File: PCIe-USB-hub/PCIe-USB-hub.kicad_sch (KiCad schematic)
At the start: 132 parts, among them J1 PCIexpress_x1, J2 USB3_A_Stacked, J3 USB3_A_Stacked, J4 USB3_A_Stacked, J5 USB3_A_Stacked, J6 USB3_A_Stacked, J7 Barrel_Jack_MountingPin

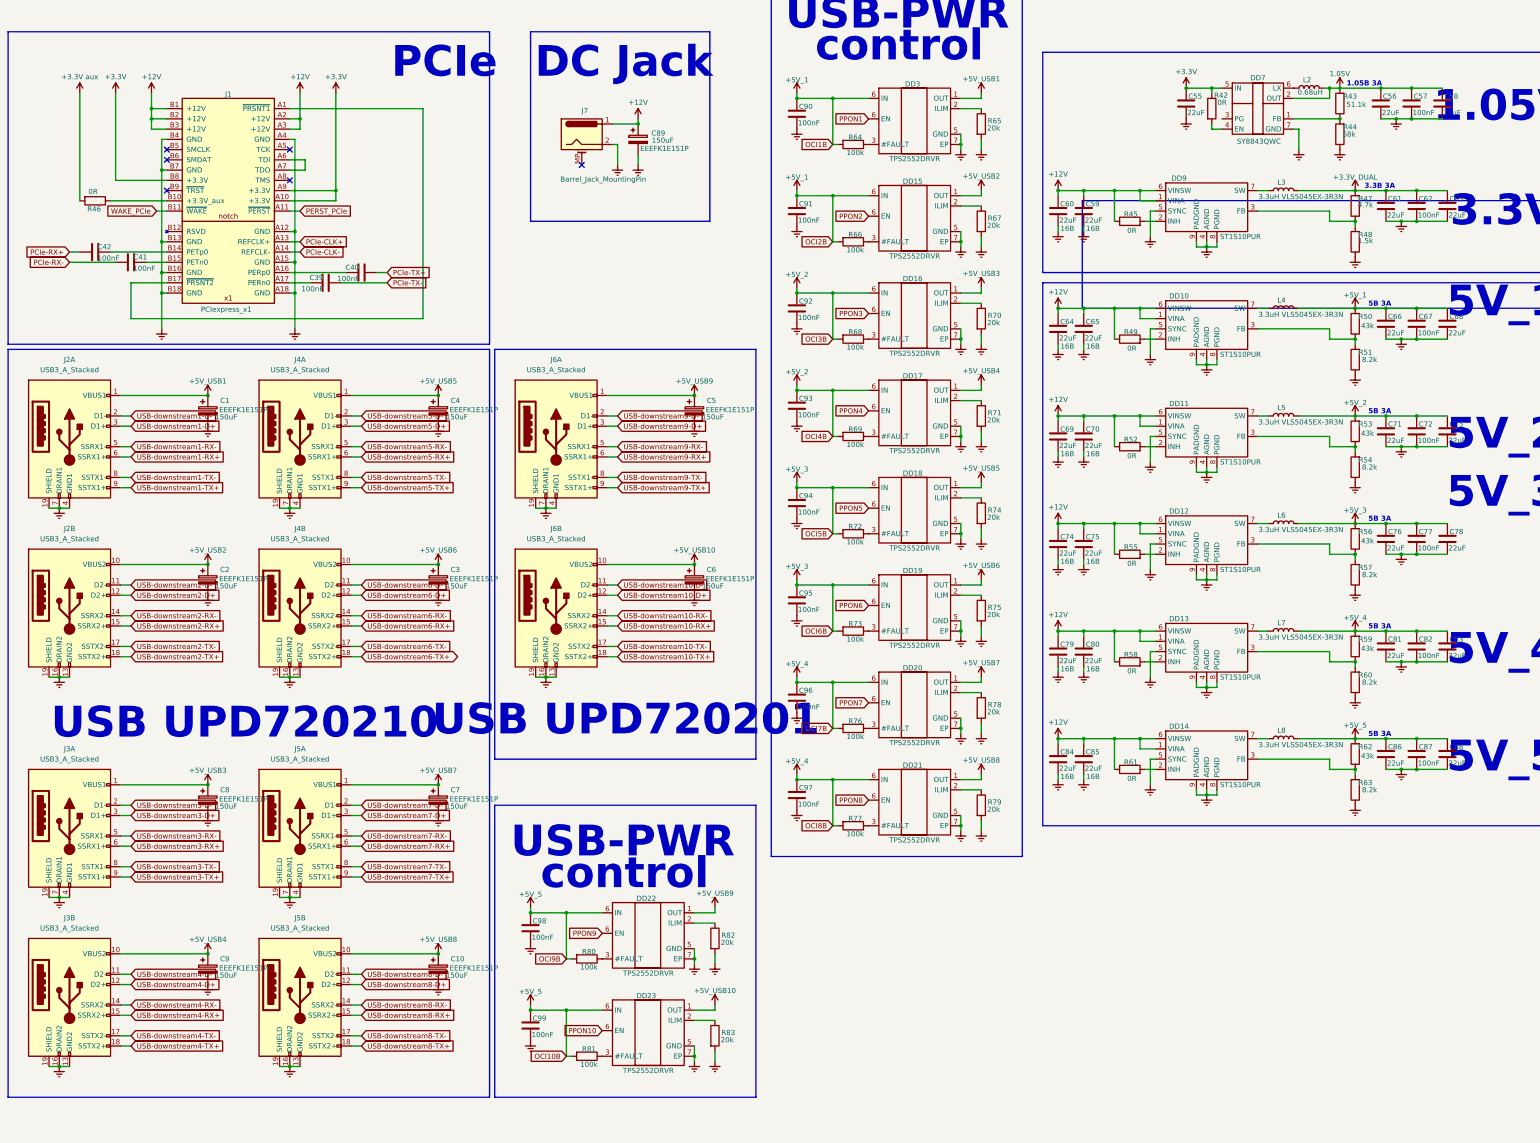
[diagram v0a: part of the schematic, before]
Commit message: тык тык поменял разъёмы на одинарные
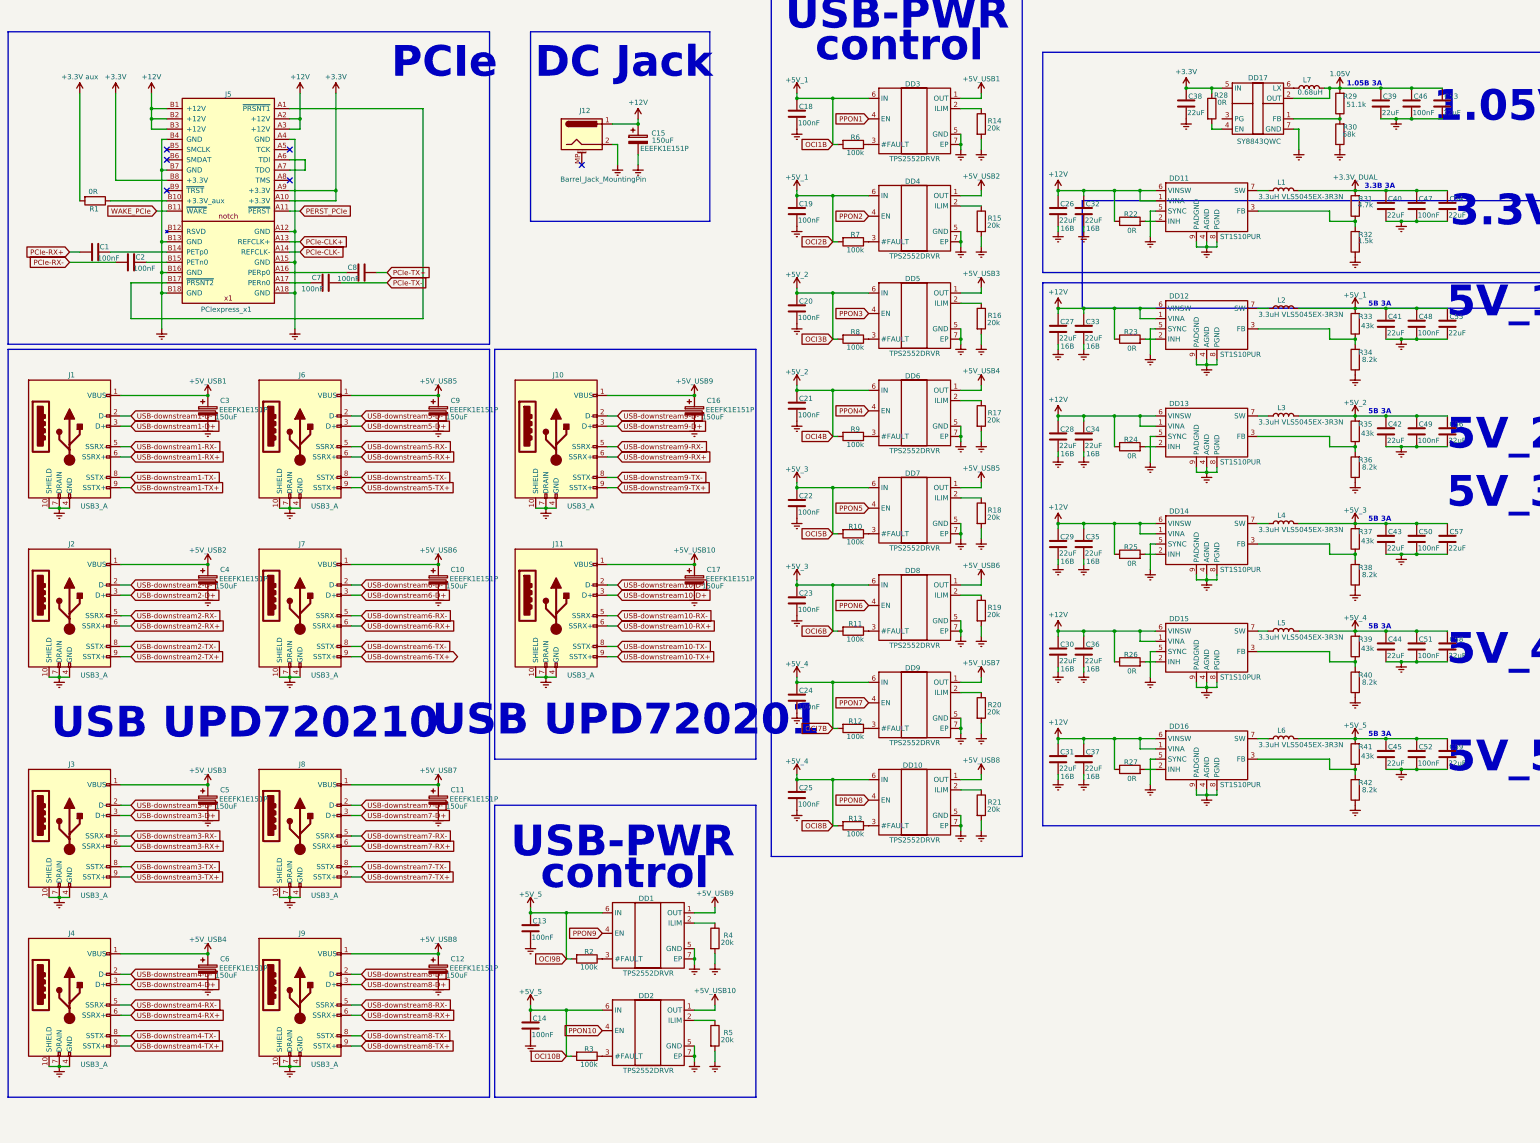
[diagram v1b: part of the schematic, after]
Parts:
- removed J2, J3, J4, J5, J6: USB3_A_Stacked, Connector_USB:USB3_A_Molex_48406-0001_Horizontal_Stacked, symbol Connector:USB3_A_Stacked
- added J1, J10, J11, J2, J3, J4, J6, J7, J8, J9: USB3_A, Connector_USB:USB3_A_Molex_48393-001, symbol Connector:USB3_A
- renumbered C42 to C1, C3 to C10, C7 to C11, C10 to C12, C98 to C13, C99 to C14, C89 to C15, C5 to C16, C6 to C17, C90 to C18, C91 to C19, C41 to C2, C92 to C20, C93 to C21, C94 to C22, C95 to C23, C96 to C24, C97 to C25, C60 to C26, C64 to C27, C69 to C28, C74 to C29, C1 to C3, C79 to C30, C84 to C31, C59 to C32, C65 to C33, C70 to C34, C75 to C35, C80 to C36, C85 to C37, C55 to C38, C56 to C39, C2 to C4, C61 to C40, C66 to C41, C71 to C42, C76 to C43, C81 to C44, C86 to C45, C57 to C46, C62 to C47, C67 to C48, C72 to C49, C8 to C5, C77 to C50, C82 to C51, C87 to C52, C58 to C53, C63 to C54, C68 to C55, C73 to C56, C78 to C57, C83 to C58, C88 to C59, C9 to C6, C39 to C7, C40 to C8, C4 to C9, DD22 to DD1, DD21 to DD10, DD9 to DD11, DD10 to DD12, DD11 to DD13, DD12 to DD14, DD13 to DD15, DD14 to DD16, DD7 to DD17, DD23 to DD2, DD15 to DD4, DD16 to DD5, DD17 to DD6, DD18 to DD7, DD19 to DD8, DD20 to DD9, J7 to J12, J1 to J5, L3 to L1, L4 to L2, L5 to L3, L6 to L4, L7 to L5, L8 to L6, L2 to L7, R46 to R1, R72 to R10, R73 to R11, R76 to R12, R77 to R13, R65 to R14, R67 to R15, R70 to R16, R71 to R17, R74 to R18, R75 to R19, R80 to R2, R78 to R20, R79 to R21, R45 to R22, R49 to R23, R52 to R24, R55 to R25, R58 to R26, R61 to R27, R42 to R28, R43 to R29, R81 to R3, R44 to R30, R47 to R31, R48 to R32, R50 to R33, R51 to R34, R53 to R35, R54 to R36, R56 to R37, R57 to R38, R59 to R39, R82 to R4, R60 to R40, R62 to R41, R63 to R42, R83 to R5, R64 to R6, R66 to R7, R68 to R8, R69 to R9
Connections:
- net +5V_USB1: now also J1.1 (VBUS)
- net +5V_USB10: now also J11.1 (VBUS)
- net +5V_USB2: now also J2.1 (VBUS)
- net +5V_USB3: now also J3.1 (VBUS)
- net +5V_USB4: now also J4.1 (VBUS)
- net +5V_USB5: now also J6.1 (VBUS)
- net +5V_USB6: now also J7.1 (VBUS)
- net +5V_USB7: now also J8.1 (VBUS)
- net +5V_USB8: now also J9.1 (VBUS)
- net +5V_USB9: now also J10.1 (VBUS)
- net Earth: now also J1.10 (SHIELD), J1.4 (GND), J1.7 (DRAIN), J10.10 (SHIELD), J10.4 (GND), J10.7 (DRAIN), J11.10 (SHIELD), J11.4 (GND), J11.7 (DRAIN), J2.10 (SHIELD), J2.4 (GND), J2.7 (DRAIN), J3.10 (SHIELD), J3.4 (GND), J3.7 (DRAIN), J4.10 (SHIELD), J4.4 (GND), J4.7 (DRAIN), J6.10 (SHIELD), J6.4 (GND), J6.7 (DRAIN), J7.10 (SHIELD), J7.4 (GND), J7.7 (DRAIN), J8.10 (SHIELD), J8.4 (GND), J8.7 (DRAIN), J9.10 (SHIELD), J9.4 (GND), J9.7 (DRAIN)
- net PPON1: now also DD3.4 (EN); no longer DD3.6 (EN)
- net PPON10: now also DD2.4 (EN); no longer DD2.6 (EN)
- net PPON2: now also DD4.4 (EN); no longer DD4.6 (EN)
- net PPON3: now also DD5.4 (EN); no longer DD5.6 (EN)
- net PPON4: now also DD6.4 (EN); no longer DD6.6 (EN)
- net PPON5: now also DD7.4 (EN); no longer DD7.6 (EN)
- net PPON6: now also DD8.4 (EN); no longer DD8.6 (EN)
- net PPON7: now also DD9.4 (EN); no longer DD9.6 (EN)
- net PPON8: now also DD10.4 (EN); no longer DD10.6 (EN)
- net PPON9: now also DD1.4 (EN); no longer DD1.6 (EN)
- net USB-downstream1-D+: now also J1.3 (D+)
- net USB-downstream1-D-: now also J1.2 (D-)
- net USB-downstream1-RX+: now also J1.6 (SSRX+)
- net USB-downstream1-RX-: now also J1.5 (SSRX-)
- net USB-downstream1-TX+: now also J1.9 (SSTX+)
- net USB-downstream1-TX-: now also J1.8 (SSTX-)
- net USB-downstream10-D+: now also J11.3 (D+)
- net USB-downstream10-D-: now also J11.2 (D-)
- net USB-downstream10-RX+: now also J11.6 (SSRX+)
- net USB-downstream10-RX-: now also J11.5 (SSRX-)
- net USB-downstream10-TX+: now also J11.9 (SSTX+)
- net USB-downstream10-TX-: now also J11.8 (SSTX-)
- net USB-downstream2-D+: now also J2.3 (D+)
- net USB-downstream2-D-: now also J2.2 (D-)
- net USB-downstream2-RX+: now also J2.6 (SSRX+)
- net USB-downstream2-RX-: now also J2.5 (SSRX-)
- net USB-downstream2-TX+: now also J2.9 (SSTX+)
- net USB-downstream2-TX-: now also J2.8 (SSTX-)
- net USB-downstream3-D+: now also J3.3 (D+)
- net USB-downstream3-D-: now also J3.2 (D-)
- net USB-downstream3-RX+: now also J3.6 (SSRX+)
- net USB-downstream3-RX-: now also J3.5 (SSRX-)
- net USB-downstream3-TX+: now also J3.9 (SSTX+)
- net USB-downstream3-TX-: now also J3.8 (SSTX-)
- net USB-downstream4-D+: now also J4.3 (D+)
- net USB-downstream4-D-: now also J4.2 (D-)
- net USB-downstream4-RX+: now also J4.6 (SSRX+)
- net USB-downstream4-RX-: now also J4.5 (SSRX-)
- net USB-downstream4-TX+: now also J4.9 (SSTX+)
- net USB-downstream4-TX-: now also J4.8 (SSTX-)
- net USB-downstream5-D+: now also J6.3 (D+)
- net USB-downstream5-D-: now also J6.2 (D-)
- net USB-downstream5-RX+: now also J6.6 (SSRX+)
- net USB-downstream5-RX-: now also J6.5 (SSRX-)
- net USB-downstream5-TX+: now also J6.9 (SSTX+)
- net USB-downstream5-TX-: now also J6.8 (SSTX-)
- net USB-downstream6-D+: now also J7.3 (D+)
- net USB-downstream6-D-: now also J7.2 (D-)
- net USB-downstream6-RX+: now also J7.6 (SSRX+)
- net USB-downstream6-RX-: now also J7.5 (SSRX-)
- net USB-downstream6-TX+: now also J7.9 (SSTX+)
- net USB-downstream6-TX-: now also J7.8 (SSTX-)
- net USB-downstream7-D+: now also J8.3 (D+)
- net USB-downstream7-D-: now also J8.2 (D-)
- net USB-downstream7-RX+: now also J8.6 (SSRX+)
- net USB-downstream7-RX-: now also J8.5 (SSRX-)
- net USB-downstream7-TX+: now also J8.9 (SSTX+)
- net USB-downstream7-TX-: now also J8.8 (SSTX-)
- net USB-downstream8-D+: now also J9.3 (D+)
- net USB-downstream8-D-: now also J9.2 (D-)
- net USB-downstream8-RX+: now also J9.6 (SSRX+)
- net USB-downstream8-RX-: now also J9.5 (SSRX-)
- net USB-downstream8-TX+: now also J9.9 (SSTX+)
- net USB-downstream8-TX-: now also J9.8 (SSTX-)
- net USB-downstream9-D+: now also J10.3 (D+)
- net USB-downstream9-D-: now also J10.2 (D-)
- net USB-downstream9-RX+: now also J10.6 (SSRX+)
- net USB-downstream9-RX-: now also J10.5 (SSRX-)
- net USB-downstream9-TX+: now also J10.9 (SSTX+)
- net USB-downstream9-TX-: now also J10.8 (SSTX-)

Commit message: натыкал трассировку всех дифф линий, поменял часть местами для удобной трассировки
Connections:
- net _PCIe-RX-: now reaches C2.2, J5.B15 (PETn0)
- net _PCIe-TX-: now reaches C7.2, J5.A17 (PERn0)
- net _PCIe-TX+: now reaches C8.2, J5.A16 (PERp0)
- net _PCIe-RX+: now reaches C1.2, J5.B14 (PETp0)
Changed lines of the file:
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@@
+		)
+	)
+	(global_label "_PCIe-RX+"
+		(shape input)
+		(at 60.96 77.47 180)
+		(fields_autoplaced yes)
+		(effects
+			(font
+				(size 0.127 0.127)
+			)
+			(justify right)
+		)
+		(property "Intersheetrefs" "${INTERSHEET_REFS}"
+			(at 59.5785 77.47 0)
+			(effects
+				(font
+					(size 1.27 1.27)
+				)
+				(justify right)
+				(hide yes)
+			)
 		)
 	)
@@
 		)
 	)
+	(global_label "_PCIe-RX-"
+		(shape input)
+		(at 60.96 80.01 180)
+		(fields_autoplaced yes)
+		(effects
+			(font
+				(size 0.127 0.127)
+			)
+			(justify right)
+		)
+		(property "Intersheetrefs" "${INTERSHEET_REFS}"
+			(at 59.5785 80.01 0)
+			(effects
+				(font
+					(size 1.27 1.27)
+				)
+				(justify right)
+				(hide yes)
+			)
+		)
+	)
 	(global_label "USB-downstream9-RX-"
 		(shape input)
@@
 		)
 	)
+	(global_label "_PCIe-TX+"
+		(shape input)
+		(at 96.52 82.55 0)
+		(fields_autoplaced yes)
+		(effects
+			(font
+				(size 0.127 0.127)
+			)
+			(justify left)
+		)
+		(property "Intersheetrefs" "${INTERSHEET_REFS}"
+			(at 97.8713 82.55 0)
+			(effects
+				(font
+					(size 1.27 1.27)
+				)
+				(justify left)
+				(hide yes)
+			)
+		)
+	)
 	(global_label "OCI6B"
 		(shape input)
@@
 		)
 	)
+	(global_label "_PCIe-TX-"
+		(shape input)
+		(at 96.52 85.09 0)
+		(fields_autoplaced yes)
+		(effects
+			(font
+				(size 0.127 0.127)
+			)
+			(justify left)
+		)
+		(property "Intersheetrefs" "${INTERSHEET_REFS}"
+			(at 97.8713 85.09 0)
+			(effects
+				(font
+					(size 1.27 1.27)
+				)
+				(justify left)
+				(hide yes)
+			)
+		)
+	)
 	(global_label "USB-downstream7-RX+"
 		(shape input)
@@
 				(justify left)
 				(hide yes)
+			)
+		)
+	)
+	(rule_area
+		(polyline
+			(pts
+				(xy 128.27 276.098) (xy 128.27 255.27) (xy 120.65 254) (xy 113.03 254) (xy 110.49 256.54) (xy 110.49 276.86)
+				(xy 113.03 279.4) (xy 120.65 279.4)
+			)
+			(stroke
+				(width 0)
+				(type dash)
+			)
+			(fill
+				(type none)
 			)
 		)
@@
 		(polyline
 			(pts
-				(xy 71.12 276.098) (xy 71.12 255.27) (xy 63.5 254) (xy 55.88 254) (xy 53.34 256.54) (xy 53.34 276.86)
-				(xy 55.88 279.4) (xy 63.5 279.4)
+				(xy 128.27 137.668) (xy 128.27 116.84) (xy 120.65 115.57) (xy 113.03 115.57) (xy 110.49 118.11)
+				(xy 110.49 138.43) (xy 113.03 140.97) (xy 120.65 140.97)
 			)
 			(stroke
@@
 		(polyline
 			(pts
-				(xy 191.77 137.668) (xy 191.77 116.84) (xy 184.15 115.57) (xy 176.53 115.57) (xy 173.99 118.11)
-				(xy 173.99 138.43) (xy 176.53 140.97) (xy 184.15 140.97)
+				(xy 71.12 276.098) (xy 71.12 255.27) (xy 63.5 254) (xy 55.88 254) (xy 53.34 256.54) (xy 53.34 276.86)
+				(xy 55.88 279.4) (xy 63.5 279.4)
+			)
+			(stroke
+				(width 0)
+				(type dash)
+			)
+			(fill
+				(type none)
+			)
+		)
+	)
+	(rule_area
+		(polyline
+			(pts
+				(xy 128.27 179.578) (xy 128.27 158.75) (xy 120.65 157.48) (xy 113.03 157.48) (xy 110.49 160.02)
+				(xy 110.49 180.34) (xy 113.03 182.88) (xy 120.65 182.88)
 			)
 			(stroke
@@
 		(polyline
 			(pts
-				(xy 128.27 137.668) (xy 128.27 116.84) (xy 120.65 115.57) (xy 113.03 115.57) (xy 110.49 118.11)
-				(xy 110.49 138.43) (xy 113.03 140.97) (xy 120.65 140.97)
-			)
-			(stroke
-				(width 0)
-				(type dash)
-			)
-			(fill
-				(type none)
-			)
-		)
-	)
-	(rule_area
-		(polyline
-			(pts
-				(xy 128.27 179.578) (xy 128.27 158.75) (xy 120.65 157.48) (xy 113.03 157.48) (xy 110.49 160.02)
-				(xy 110.49 180.34) (xy 113.03 182.88) (xy 120.65 182.88)
+				(xy 71.12 179.578) (xy 71.12 158.75) (xy 63.5 157.48) (xy 55.88 157.48) (xy 53.34 160.02) (xy 53.34 180.34)
+				(xy 55.88 182.88) (xy 63.5 182.88)
 			)
 			(stroke
@@
 		(polyline
 			(pts
-				(xy 71.12 179.578) (xy 71.12 158.75) (xy 63.5 157.48) (xy 55.88 157.48) (xy 53.34 160.02) (xy 53.34 180.34)
-				(xy 55.88 182.88) (xy 63.5 182.88)
+				(xy 191.77 137.668) (xy 191.77 116.84) (xy 184.15 115.57) (xy 176.53 115.57) (xy 173.99 118.11)
+				(xy 173.99 138.43) (xy 176.53 140.97) (xy 184.15 140.97)
 			)
 			(stroke
-				(width 0)
-				(type dash)
-			)
-			(fill
-				(type none)
-			)
-		)
-	)
-	(rule_area
-		(polyline
-			(pts
-				(xy 128.27 276.098) (xy 128.27 255.27) (xy 120.65 254) (xy 113.03 254) (xy 110.49 256.54) (xy 110.49 276.86)
-				(xy 113.03 279.4) (xy 120.65 279.4)
-			)
-			(stroke

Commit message: тык-перетык
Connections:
- net OCI10B: now reaches DD2.3 (#FAULT), R3.1
- net OCI8B: now reaches DD10.3 (#FAULT), R13.1
- net OCI5B: now reaches DD7.3 (#FAULT), R10.1
- net OCI9B: now reaches DD1.3 (#FAULT), R2.1
- net OCI1B: now reaches DD3.3 (#FAULT), R6.1
- net OCI7B: now reaches DD9.3 (#FAULT), R12.1
- net OCI3B: now reaches DD5.3 (#FAULT), R8.1
- net OCI4B: now reaches DD6.3 (#FAULT), R9.1
- net OCI6B: now reaches DD8.3 (#FAULT), R11.1
- net OCI2B: now reaches DD4.3 (#FAULT), R7.1
